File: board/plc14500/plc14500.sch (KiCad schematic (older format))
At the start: 58 parts

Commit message: Schema
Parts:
- removed C? (x3): C, symbol Device:C
- removed C? (x4): 100nF, symbol Device:C
- removed D? (x19): LED5MM, LED_5MM, symbol SparkFun-LED:LED5MM
- removed R? (x21): 680R, symbol Device:R
- removed R? (x2): 10K, symbol Device:R
- removed R?: 1M, symbol Device:R
- removed S? (x2): SWITCH-DPDT-PTH-GPI-152-3013, SWITCH_DPDT_PTH_GPI-152-3013, symbol SparkFun-Switches:SWITCH-DPDT-PTH-GPI-152-3013
- removed SW?: SW_Push, symbol Switch:SW_Push
- removed U?: NE555, Package_DIP:DIP-8_W7.62mm, symbol SparkFun-IC-Special-Function:555D
- removed U?: 74HC590A, symbol 74xx:74HC590A
- removed U?: 74HC14, symbol 74xx:74HC14
- removed U?: LH5168, Package_DIP:DIP-28_W15.24mm, symbol Memory_RAM:KM62256CLP
- removed U?: MC14500, symbol plc14500:MC14500
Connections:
- no-connect marks 3 -> 0
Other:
- note removed: "*1"
- note removed: "*1) Why A13 to one? This allows to use both 32Kx8 and 8Kx8 (that have pin 13 as a second CE)"
- note removed: "Clock"
- note removed: "HI"
- note removed: "LO"
- note removed: "Program Counter"
- note removed: "RUN"
- note removed: "STEP"

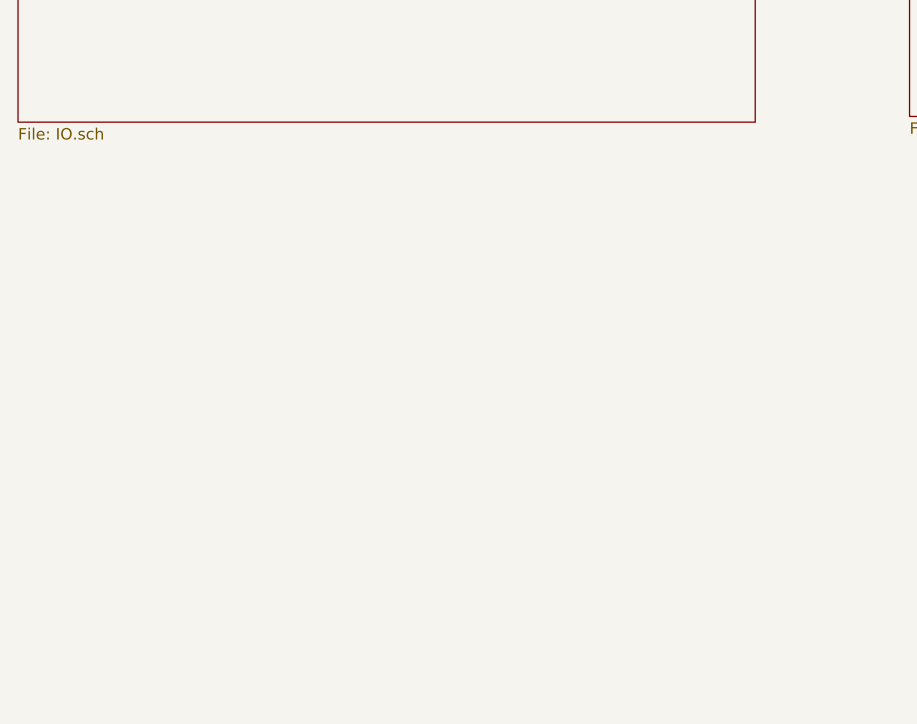
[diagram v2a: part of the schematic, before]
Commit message: Add scratchpad ram
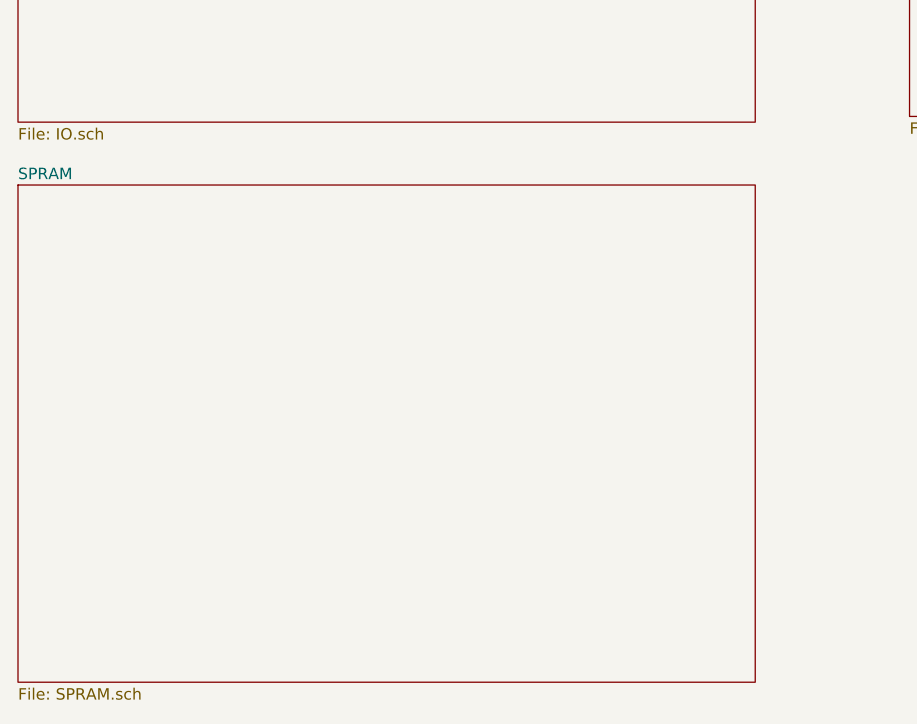
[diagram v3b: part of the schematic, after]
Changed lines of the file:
@@
 $Descr A4 11693 8268
 encoding utf-8
-Sheet 1 3
+Sheet 1 4
 Title "PLC14500 - Nano"
 Date "2022-11-07"
@@
 F1 "CPU.sch" 50
 $EndSheet
+$Sheet
+S 1275 3850 3225 2175
+U 67425B3B
+F0 "SPRAM" 50
+F1 "SPRAM.sch" 50
+$EndSheet
 $EndSCHEMATC

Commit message: Schematic tweaks
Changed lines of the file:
@@
 Sheet 1 4
 Title "PLC14500 - Nano"
-Date "2022-11-07"
-Rev "0.3"
+Date "2022-11-09"
+Rev "0.4"
 Comp "Nicola Cimmino"
 Comment1 ""
@@
 F1 "SPRAM.sch" 50
 $EndSheet
+$Comp
+L power:GND #PWR?
+U 1 1 6817676E
+P 9075 2100
+AR Path="/67425B3B/6817676E" Ref="#PWR?"  Part="1"
+AR Path="/6817676E" Ref="#PWR02"  Part="1"
+F 0 "#PWR02" H 9075 1850 50  0001 C CNN
+F 1 "GND" H 9080 1927 50  0000 C CNN
+F 2 "" H 9075 2100 50  0001 C CNN
+F 3 "" H 9075 2100 50  0001 C CNN
+	1    9075 2100
+	1    0    0    -1
+$EndComp
+$Comp
+L power:PWR_FLAG #FLG?
+U 1 1 68176774
+P 9075 2025
+AR Path="/67425B3B/68176774" Ref="#FLG?"  Part="1"
+AR Path="/68176774" Ref="#FLG02"  Part="1"
+F 0 "#FLG02" H 9075 2100 50  0001 C CNN
+F 1 "PWR_FLAG" H 9075 2198 50  0001 C CNN
+F 2 "" H 9075 2025 50  0001 C CNN
+F 3 "~" H 9075 2025 50  0001 C CNN
+	1    9075 2025
+	1    0    0    -1
+$EndComp
+Wire Wire Line
+	9075 2100 9075 2025
+$Comp
+L power:PWR_FLAG #FLG?
+U 1 1 6817677B
+P 9075 1700
+AR Path="/67425B3B/6817677B" Ref="#FLG?"  Part="1"
+AR Path="/6817677B" Ref="#FLG01"  Part="1"
+F 0 "#FLG01" H 9075 1775 50  0001 C CNN
+F 1 "PWR_FLAG" H 9075 1873 50  0001 C CNN
+F 2 "" H 9075 1700 50  0001 C CNN
+F 3 "~" H 9075 1700 50  0001 C CNN
+	1    9075 1700
+	-1   0    0    1
+$EndComp
+$Comp
+L power:+5V #PWR01
+U 1 1 68176781
+P 9075 1625
+AR Path="/68176781" Ref="#PWR01"  Part="1"
+AR Path="/63B4BDA9/68176781" Ref="#PWR?"  Part="1"
+AR Path="/67425B3B/68176781" Ref="#PWR?"  Part="1"
+F 0 "#PWR01" H 9075 1475 50  0001 C CNN
+F 1 "+5V" H 9090 1798 50  0000 C CNN
+F 2 "" H 9075 1625 50  0001 C CNN
+F 3 "" H 9075 1625 50  0001 C CNN
+	1    9075 1625
+	1    0    0    -1
+$EndComp
+Wire Wire Line
+	9075 1700 9075 1625
 $EndSCHEMATC

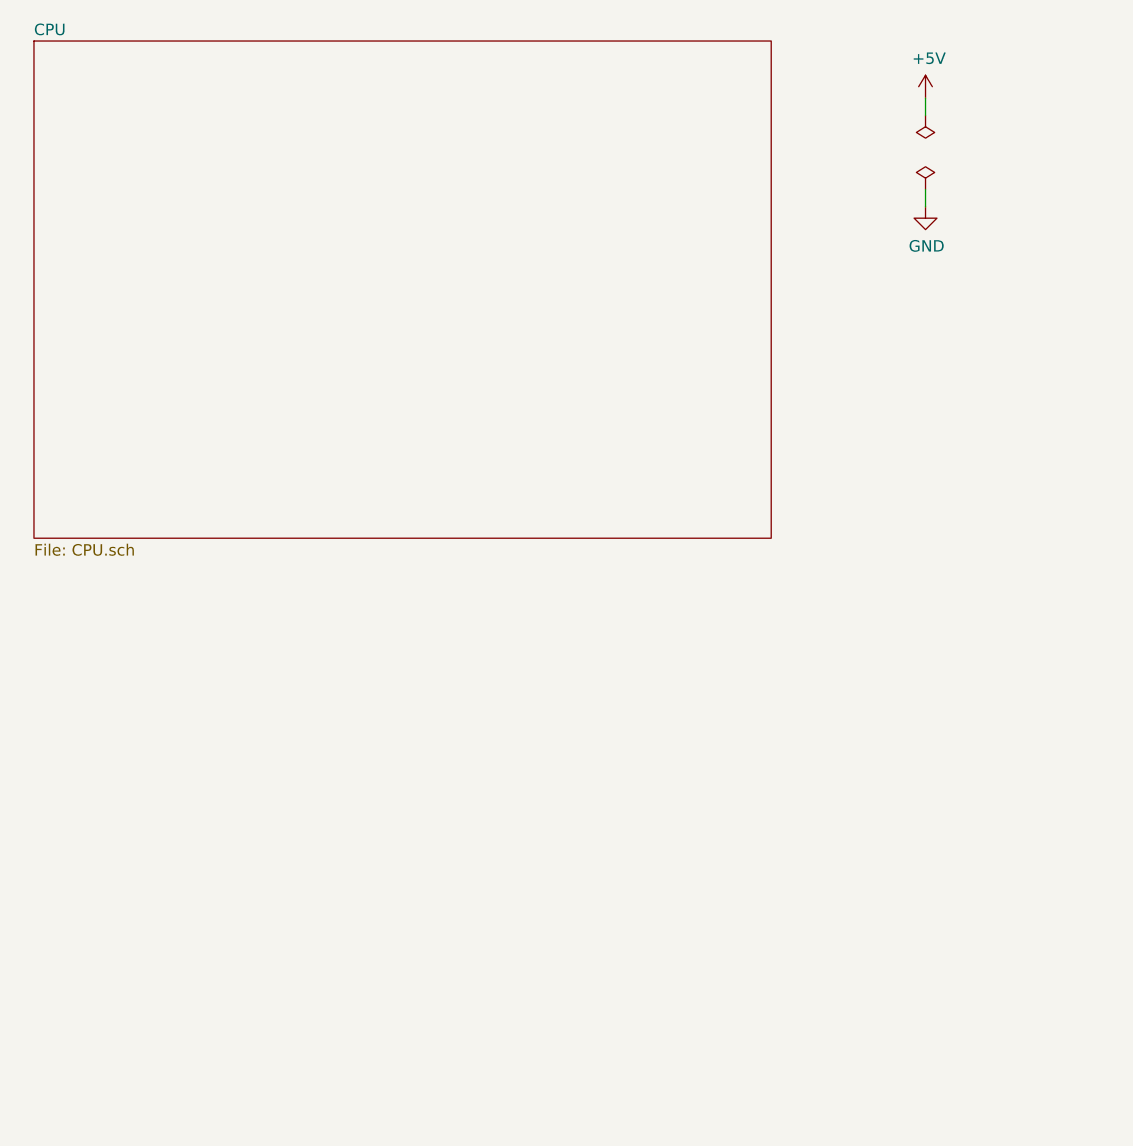
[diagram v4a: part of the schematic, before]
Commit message: All components on the board! WIP
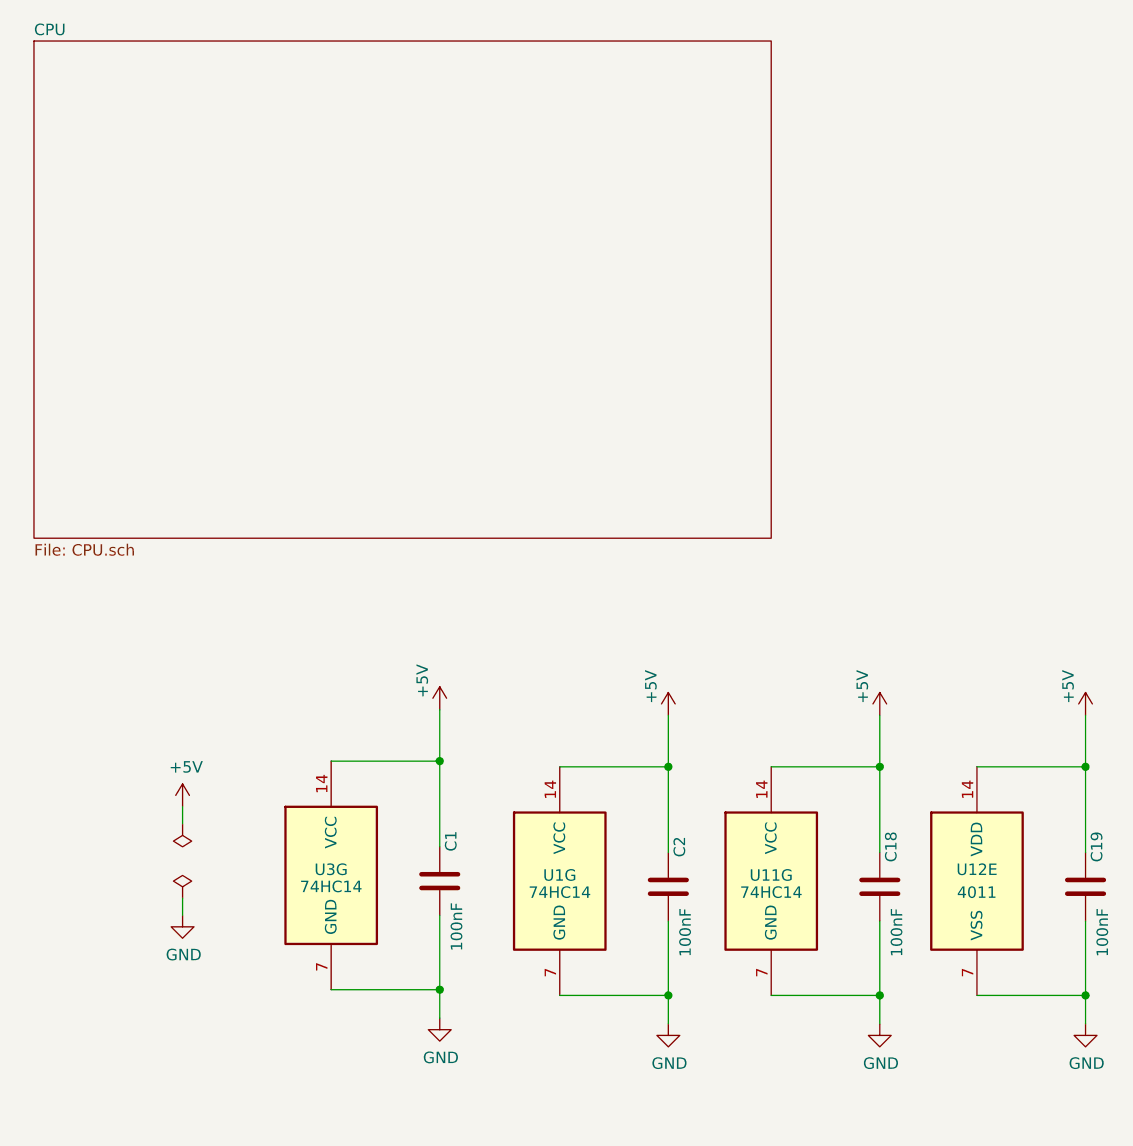
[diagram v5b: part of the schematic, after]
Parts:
- added C1, C18, C19, C2: 100nF, Capacitor_THT:C_Rect_L7.2mm_W2.5mm_P5.00mm_FKS2_FKP2_MKS2_MKP2, symbol Device:C
- added U1, U11, U3: 74HC14, Package_DIP:DIP-14_W7.62mm_LongPads, symbol 74xx:74HC14
- added U12: 4011, Package_DIP:DIP-14_W7.62mm_LongPads, symbol 4xxx:4011
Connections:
- net +5V: now also C1.2, C18.2, C19.2, C2.2, U1.14 (VCC), U11.14 (VCC), U12.14 (VDD), U3.14 (VCC)
- net GND: now also C1.1, C18.1, C19.1, C2.1, U1.7 (GND), U11.7 (GND), U12.7 (VSS), U3.7 (GND)
